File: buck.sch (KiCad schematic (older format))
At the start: 23 parts, among them U3 MD7133H, U5 MP1584EN, U6 INA199A1DCKR

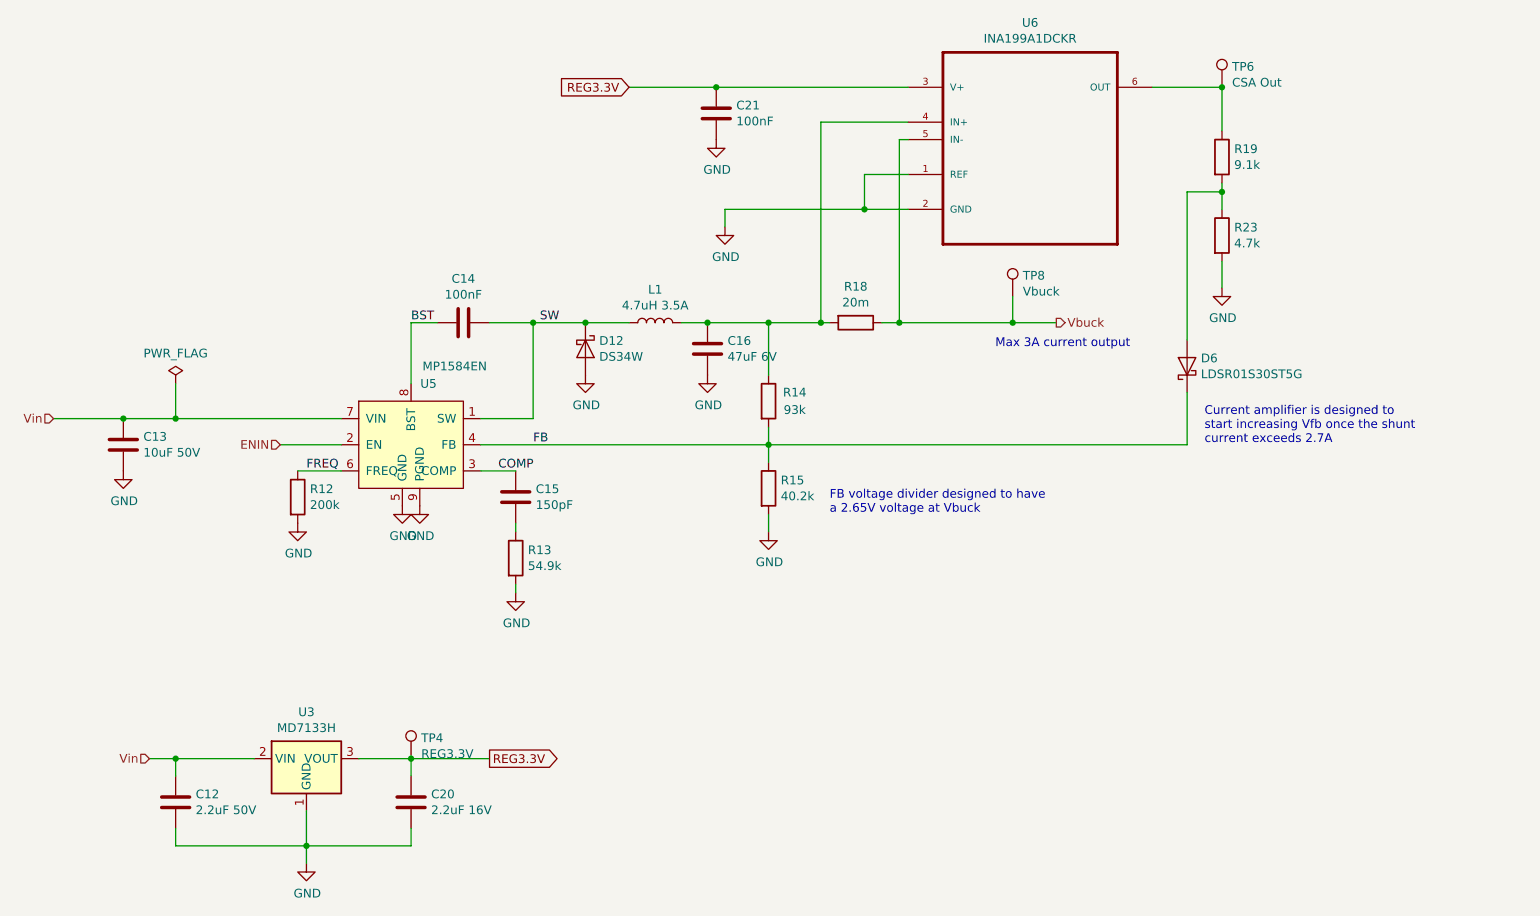
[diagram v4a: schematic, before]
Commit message: Update licence, tweaks to footprints and ERC
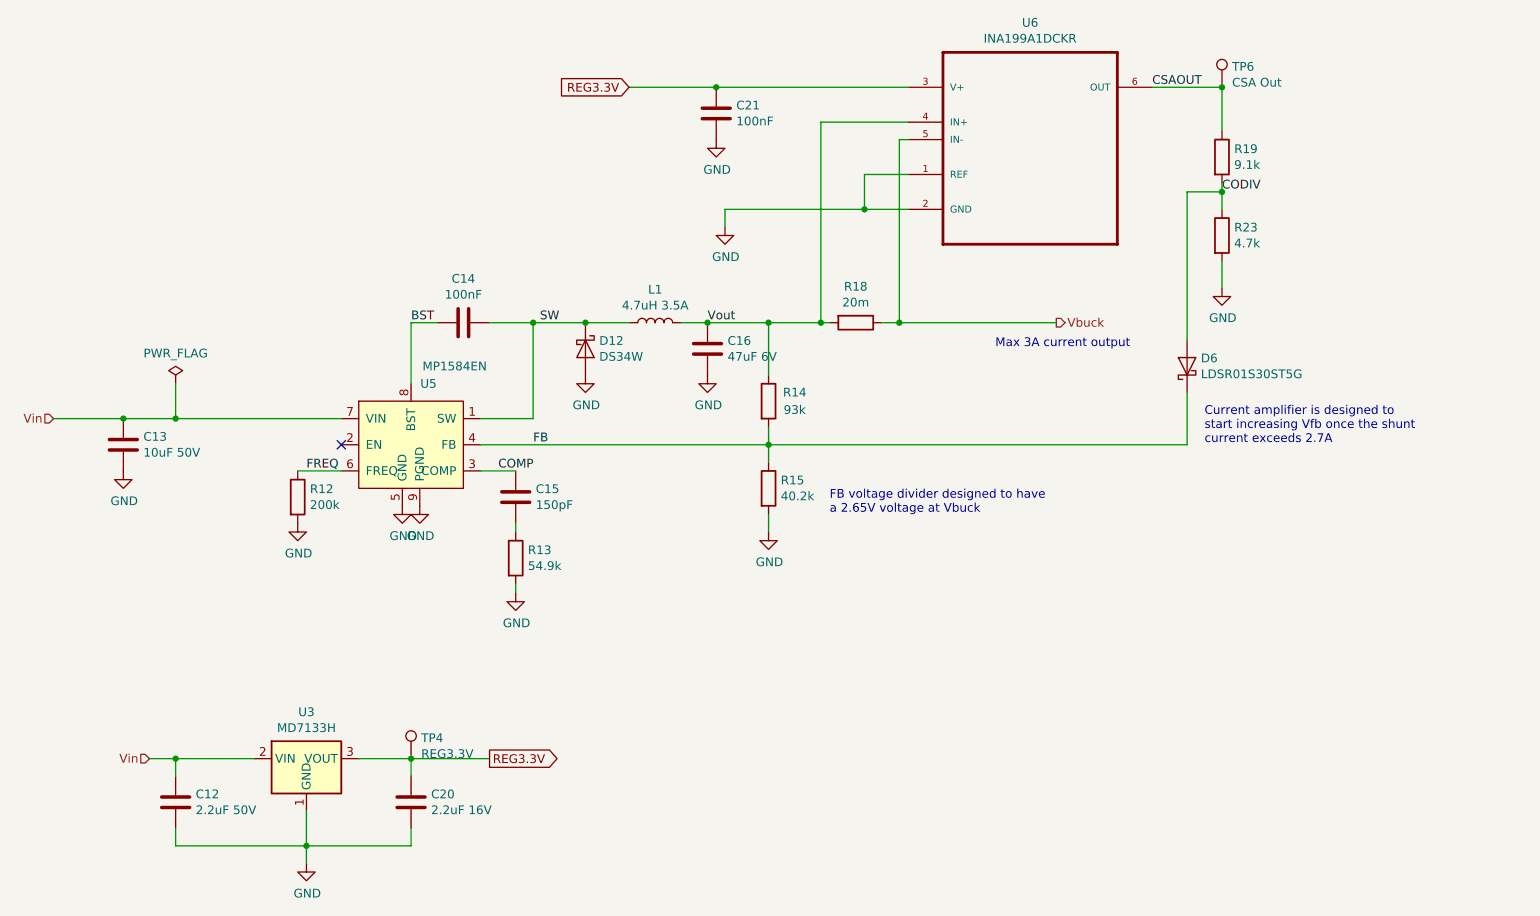
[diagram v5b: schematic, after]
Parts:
- removed TP8: Vbuck, TestPoint:TestPoint_Keystone_5000-5004_Miniature, symbol Connector:TestPoint
- C12: footprint (none) -> Capacitor_SMD:C_1206_3216Metric
- C16: footprint Capacitor_SMD:C_0805_2012Metric_Pad1.15x1.40mm_HandSolder -> Capacitor_SMD:C_1210_3225Metric
- C20, C21: footprint (none) -> Capacitor_SMD:C_0603_1608Metric_Pad1.05x0.95mm_HandSolder
- D6: footprint (none) -> Diode_SMD:D_0603_1608Metric
- R18: footprint (none) -> Resistor_SMD:R_1206_3216Metric_Pad1.42x1.75mm_HandSolder
- R19, R23: footprint (none) -> Resistor_SMD:R_0603_1608Metric_Pad1.05x0.95mm_HandSolder
- TP4, TP6: footprint (none) -> TestPoint:TestPoint_Keystone_5000-5004_Miniature
- U6: footprint SOT65P210X110-6N -> custom:SOT65P210X110-6N
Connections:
- net Vout: now reaches C16.1, L1.2, R14.1, R18.2, U6.4 (IN+)
- net CSAOUT: now reaches R19.1, TP6.1, U6.6 (OUT)
- net CODIV: now reaches D6.2 (A), R19.2, R23.1
- net ENIN: no longer names the net of U5.2 (EN)
- no-connect marks 0 -> 1
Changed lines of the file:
@@
 $Descr A4 11693 8268
 encoding utf-8
-Sheet 5 6
+Sheet 5 7
 Title ""
 Date ""
@@
 F 0 "C16" H 4765 2846 50  0000 L CNN
 F 1 "47uF 6V" H 4765 2755 50  0000 L CNN
-F 2 "Capacitor_SMD:C_0805_2012Metric_Pad1.15x1.40mm_HandSolder" H 4688 2650 50  0001 C CNN
+F 2 "Capacitor_SMD:C_1210_3225Metric" H 4688 2650 50  0001 C CNN
 F 3 "~" H 4650 2800 50  0001 C CNN
 F 4 "Min 6.3V" H 4650 2800 50  0001 C CNN "Notes"
@@
 	4650 2650 5000 2650
 $Comp
-L Connector:TestPoint TP?
-U 1 1 5CAACEED
-P 6400 2500
-AR Path="/5C345D5A/5CAACEED" Ref="TP?"  Part="1"
-AR Path="/5CA65CC5/5CAACEED" Ref="TP8"  Part="1"
-F 0 "TP8" H 6458 2620 50  0000 L CNN
-F 1 "Vbuck" H 6458 2529 50  0000 L CNN
-F 2 "TestPoint:TestPoint_Keystone_5000-5004_Miniature" H 6600 2500 50  0001 C CNN
-F 3 "~" H 6600 2500 50  0001 C CNN
-	1    6400 2500
-	1    0    0    -1
-$EndComp
-$Comp
 L power:GND #PWR?
 U 1 1 5CA8A650
@@
 Text Notes 5350 3750 0    50   ~ 0
 FB voltage divider designed to have\na 2.65V voltage at Vbuck
-Wire Wire Line
-	6400 2500 6400 2650
-Connection ~ 6400 2650
-Wire Wire Line
-	6400 2650 6650 2650
 Text Notes 6300 2800 0    50   ~ 0
 Max 3A current output
@@
 F 0 "U6" H 6500 2070 50  0000 C CNN
 F 1 "INA199A1DCKR" H 6500 1979 50  0000 C CNN
-F 2 "SOT65P210X110-6N" H 6500 1500 50  0001 L BNN
+F 2 "custom:SOT65P210X110-6N" H 6500 1500 50  0001 L BNN
 F 3 "74R6382" H 6500 1500 50  0001 L BNN
 F 4 "SC70-6" H 6500 1500 50  0001 L BNN "Field4"
@@
 F 0 "C21" H 4815 1496 50  0000 L CNN
 F 1 "100nF" H 4815 1405 50  0000 L CNN
-F 2 "" H 4738 1300 50  0001 C CNN
+F 2 "Capacitor_SMD:C_0603_1608Metric_Pad1.05x0.95mm_HandSolder" H 4738 1300 50  0001 C CNN
 F 3 "~" H 4700 1450 50  0001 C CNN
 	1    4700 1450
@@
 F 0 "R18" V 5293 2650 50  0000 C CNN
 F 1 "20m" V 5384 2650 50  0000 C CNN
-F 2 "" V 5430 2650 50  0001 C CNN
+F 2 "Resistor_SMD:R_1206_3216Metric_Pad1.42x1.75mm_HandSolder" V 5430 2650 50  0001 C CNN
 F 3 "~" H 5500 2650 50  0001 C CNN
 	1    5500 2650
@@
 	5750 1600 5800 1600
 Connection ~ 5750 2650
-Wire Wire Line
-	5750 2650 6400 2650
 Wire Wire Line
 	7400 3350 5000 3350
@@
 F 0 "R19" H 7670 1746 50  0000 L CNN
 F 1 "9.1k" H 7670 1655 50  0000 L CNN
-F 2 "" V 7530 1700 50  0001 C CNN
+F 2 "Resistor_SMD:R_0603_1608Metric_Pad1.05x0.95mm_HandSolder" V 7530 1700 50  0001 C CNN
 F 3 "~" H 7600 1700 50  0001 C CNN
 	1    7600 1700
@@
 F 0 "R23" H 7670 2196 50  0000 L CNN
 F 1 "4.7k" H 7670 2105 50  0000 L CNN
-F 2 "" V 7530 2150 50  0001 C CNN
+F 2 "Resistor_SMD:R_0603_1608Metric_Pad1.05x0.95mm_HandSolder" V 7530 2150 50  0001 C CNN
 F 3 "~" H 7600 2150 50  0001 C CNN
 	1    7600 2150
@@
 F 0 "D6" V 7446 2821 50  0000 R CNN
 F 1 "LDSR01S30ST5G" V 7355 2821 50  0000 R CNN
-F 2 "" H 7400 2900 50  0001 C CNN
+F 2 "Diode_SMD:D_0603_1608Metric" H 7400 2900 50  0001 C CNN
 F 3 "~" H 7400 2900 50  0001 C CNN
 	1    7400 2900
@@
 F 0 "C12" H 1715 5446 50  0000 L CNN
 F 1 "2.2uF 50V" H 1715 5355 50  0000 L CNN
-F 2 "" H 1638 5250 50  0001 C CNN
+F 2 "Capacitor_SMD:C_1206_3216Metric" H 1638 5250 50  0001 C CNN
 F 3 "~" H 1600 5400 50  0001 C CNN
 	1    1600 5400
@@
 F 0 "C20" H 3065 5446 50  0000 L CNN
 F 1 "2.2uF 16V" H 3065 5355 50  0000 L CNN
-F 2 "" H 2988 5250 50  0001 C CNN
+F 2 "Capacitor_SMD:C_0603_1608Metric_Pad1.05x0.95mm_HandSolder" H 2988 5250 50  0001 C CNN
 F 3 "~" H 2950 5400 50  0001 C CNN
 	1    2950 5400
@@
 Text GLabel 3400 5150 2    50   Output ~ 0
 REG3.3V
-Text HLabel 2200 3350 0    50   Input ~ 0
-ENIN
-Wire Wire Line
-	2200 3350 2550 3350
 $Comp
 L Connector:TestPoint TP6
@@
 F 0 "TP6" H 7658 1418 50  0000 L CNN
 F 1 "CSA Out" H 7658 1327 50  0000 L CNN
-F 2 "" H 7800 1300 50  0001 C CNN
+F 2 "TestPoint:TestPoint_Keystone_5000-5004_Miniature" H 7800 1300 50  0001 C CNN
 F 3 "~" H 7800 1300 50  0001 C CNN
 	1    7600 1300
@@
 F 0 "TP4" H 3008 5268 50  0000 L CNN
 F 1 "REG3.3V" H 3008 5177 50  0000 L CNN
-F 2 "" H 3150 5150 50  0001 C CNN
+F 2 "TestPoint:TestPoint_Keystone_5000-5004_Miniature" H 3150 5150 50  0001 C CNN
 F 3 "~" H 3150 5150 50  0001 C CNN
 	1    2950 5150
 	1    0    0    -1
 $EndComp
+Wire Wire Line
+	5750 2650 6650 2650
+Text Label 4650 2650 0    50   ~ 0
+Vout
+Text Label 7200 1300 0    50   ~ 0
+CSAOUT
+Text Label 7600 1900 0    50   ~ 0
+CODIV
+NoConn ~ 2550 3350
 $EndSCHEMATC

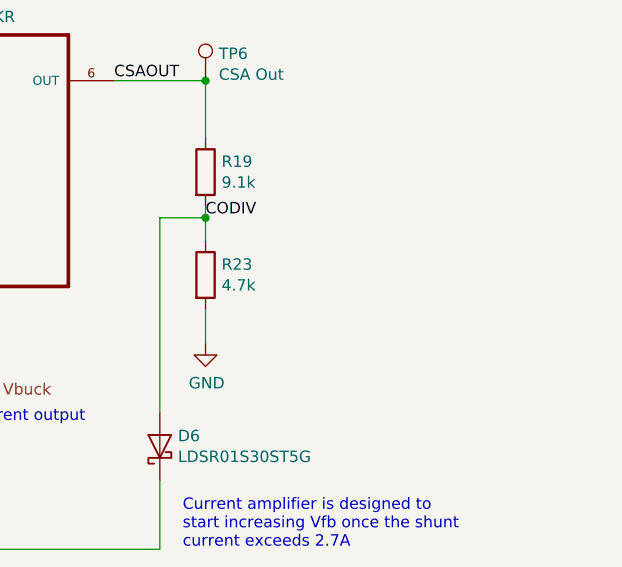
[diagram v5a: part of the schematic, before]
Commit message: Need a cap to cool down current limiting FB loop
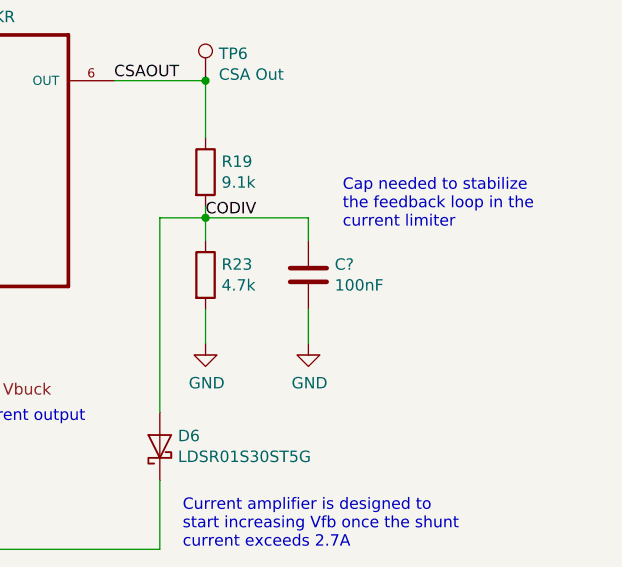
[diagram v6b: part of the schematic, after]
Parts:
- added C?: 100nF, Capacitor_SMD:C_0603_1608Metric_Pad1.05x0.95mm_HandSolder, symbol Device:C
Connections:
- net CODIV: now also C?.1
- net GND: now also C?.2
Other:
- note added: "Cap needed to stabilize\nthe feedback loop in the \ncurrent limiter"
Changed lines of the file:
@@
 CODIV
 NoConn ~ 2550 3350
+$Comp
+L Device:C C?
+U 1 1 5E563B66
+P 8050 2150
+F 0 "C?" H 8165 2196 50  0000 L CNN
+F 1 "100nF" H 8165 2105 50  0000 L CNN
+F 2 "Capacitor_SMD:C_0603_1608Metric_Pad1.05x0.95mm_HandSolder" H 8088 2000 50  0001 C CNN
+F 3 "~" H 8050 2150 50  0001 C CNN
+	1    8050 2150
+	1    0    0    -1
+$EndComp
+Wire Wire Line
+	7600 1900 8050 1900
+Wire Wire Line
+	8050 1900 8050 2000
+$Comp
+L power:GND #PWR?
+U 1 1 5E566874
+P 8050 2450
+AR Path="/5E566874" Ref="#PWR?"  Part="1"
+AR Path="/5C3476D8/5E566874" Ref="#PWR?"  Part="1"
+AR Path="/5CA65CC5/5E566874" Ref="#PWR?"  Part="1"
+F 0 "#PWR?" H 8050 2200 50  0001 C CNN
+F 1 "GND" H 8055 2277 50  0000 C CNN
+F 2 "" H 8050 2450 50  0001 C CNN
+F 3 "" H 8050 2450 50  0001 C CNN
+	1    8050 2450
+	1    0    0    -1
+$EndComp
+Wire Wire Line
+	8050 2450 8050 2300
+Text Notes 8200 1950 0    50   ~ 0
+Cap needed to stabilize\nthe feedback loop in the \ncurrent limiter
 $EndSCHEMATC

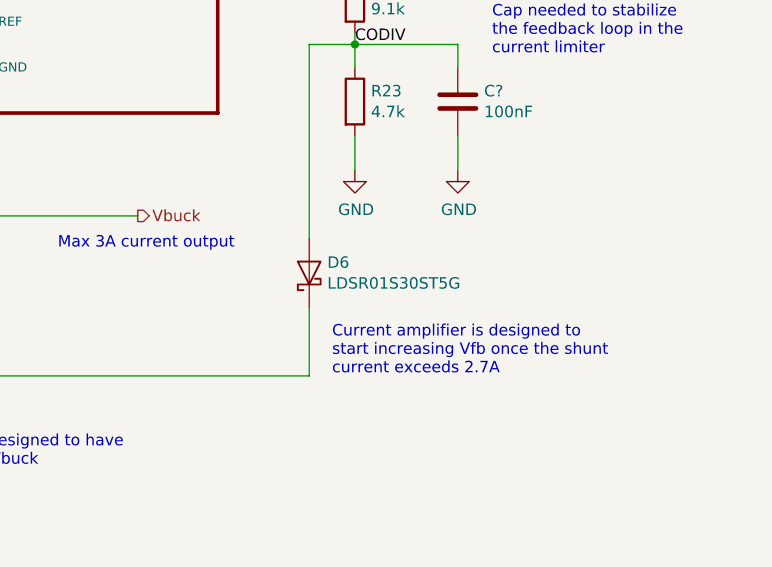
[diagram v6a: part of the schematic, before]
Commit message: Fix diode footprint
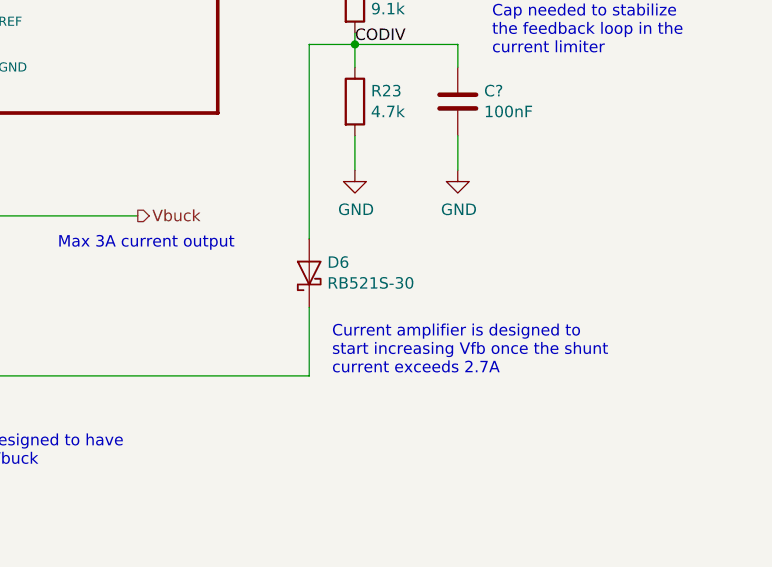
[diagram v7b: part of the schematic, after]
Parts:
- D6: value LDSR01S30ST5G -> RB521S-30; footprint Diode_SMD:D_0603_1608Metric -> Diode_SMD:D_SOD-523
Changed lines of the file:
@@
 P 7400 2900
 F 0 "D6" V 7446 2821 50  0000 R CNN
-F 1 "LDSR01S30ST5G" V 7355 2821 50  0000 R CNN
-F 2 "Diode_SMD:D_0603_1608Metric" H 7400 2900 50  0001 C CNN
+F 1 "RB521S-30" V 7355 2821 50  0000 R CNN
+F 2 "Diode_SMD:D_SOD-523" H 7400 2900 50  0001 C CNN
 F 3 "~" H 7400 2900 50  0001 C CNN
 	1    7400 2900
